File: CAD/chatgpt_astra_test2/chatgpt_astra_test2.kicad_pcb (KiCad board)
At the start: 4 copper layers, 100 x 80 mm, 97 parts, among them J1 18-30 V DC, J2 CURRENT INPUT, J3 CURRENT OUTPUT, J4 USB-C, J5 UART / 3.3 V ONLY, Q1 2N7002, Q2 2N7002, Q3 IRF9540NPBF, Q4 MMBT3906, SW1 RESET, SW2 BOOT, U1 TPS26600PWPR, U10 ADS1115IDGSR, U11 DAC80501ZDGSR, U12 XTR111AIDGQR, U2 LMR36510ADDAR, U3 LT3092EST#PBF, U4 ESP32-S3-WROOM-1-N8, U5 TPS3839G33DBZR, U6 USBLC6-2SC6, U7 LT3092EST#PBF, U8 LM4040AIM3-3.0, U9 TMUX1511PWR

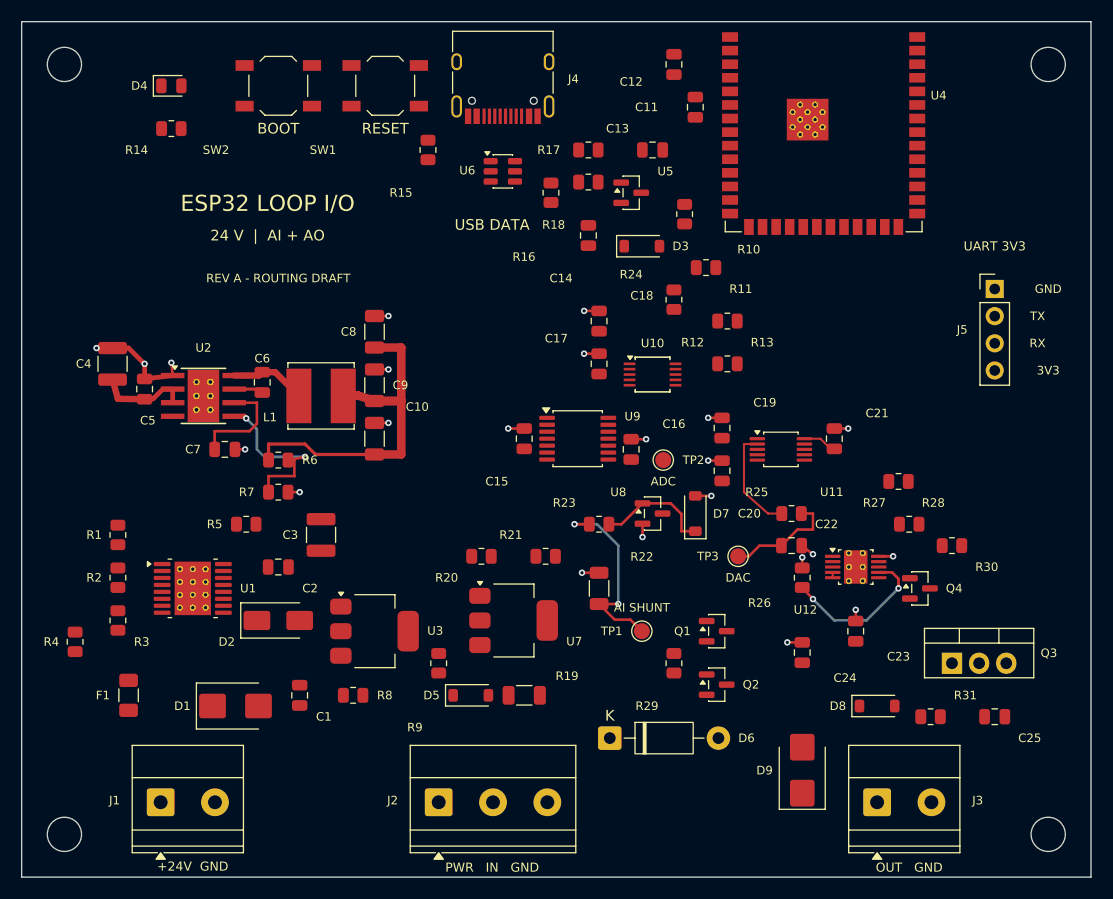
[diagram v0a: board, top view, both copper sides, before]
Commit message: Route remaining board networks with protected analog paths
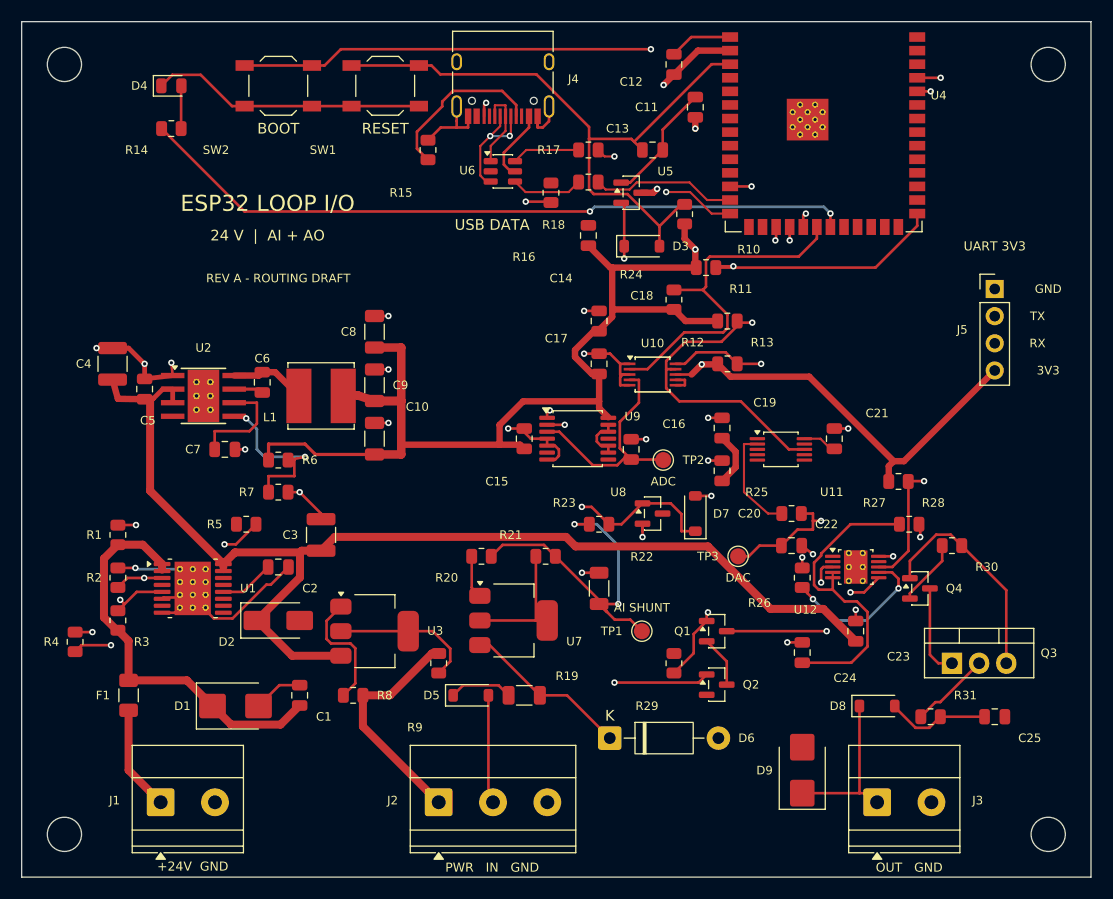
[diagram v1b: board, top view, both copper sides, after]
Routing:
- net V3V3: track 34.8 -> 188.3 mm, vias 0 -> 5
- net V24_PROT: track 8.63 -> 109.1 mm
- net GND: track 37.8 -> 124.8 mm
- net /03 / ESP32 AND USB/BOOT_N: track 0.00 -> 85.4 mm, vias 0 -> 2
- net /03 / ESP32 AND USB/LED_STATUS: track 0.00 -> 67.5 mm, vias 0 -> 2
- net /03 / ESP32 AND USB/ESP_EN: track 0.00 -> 60.9 mm
- net SYS_OK: track 0.00 -> 60.1 mm, vias 0 -> 3
- net /02 / POWER AND SENSOR SUPPLY/EF_RTN: track 0.00 -> 52.5 mm, vias 0 -> 3
- net AO_ENABLE: track 0.00 -> 46.4 mm, vias 0 -> 2
- net I2C_SDA: track 0.00 -> 43.4 mm, vias 0 -> 2
- net AO_FAULT_N: track 0.00 -> 42.4 mm, vias 0 -> 2
- net /02 / POWER AND SENSOR SUPPLY/VIN_FUSED: track 0.00 -> 38.2 mm
- net ADC_RDY: track 0.00 -> 33.1 mm
- net /05 / PRECISION CURRENT OUTPUT/XTR_GATE: track 0.00 -> 29.4 mm, vias 0 -> 1
- net /05 / PRECISION CURRENT OUTPUT/XTR_REG: track 0.50 -> 29.3 mm
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
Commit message: Add D2 ground stitch and document remaining layout work
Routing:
- net GND: track 124.8 -> 125.9 mm, vias 23 -> 24
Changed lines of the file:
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@@
+	)
+	(segment
+		(start 76 106)
+		(end 77.1 106)
+		(width 0.2)
+		(layer "F.Cu")
+		(net 52)
 	)
 	(segment
@@
 		(size 0.6)
 		(drill 0.3)
+		(layers "F.Cu" "B.Cu")
+		(net 52)
+	)
+	(via
+		(at 77.1 106)
+		(size 0.6)
+		(drill 0.3)

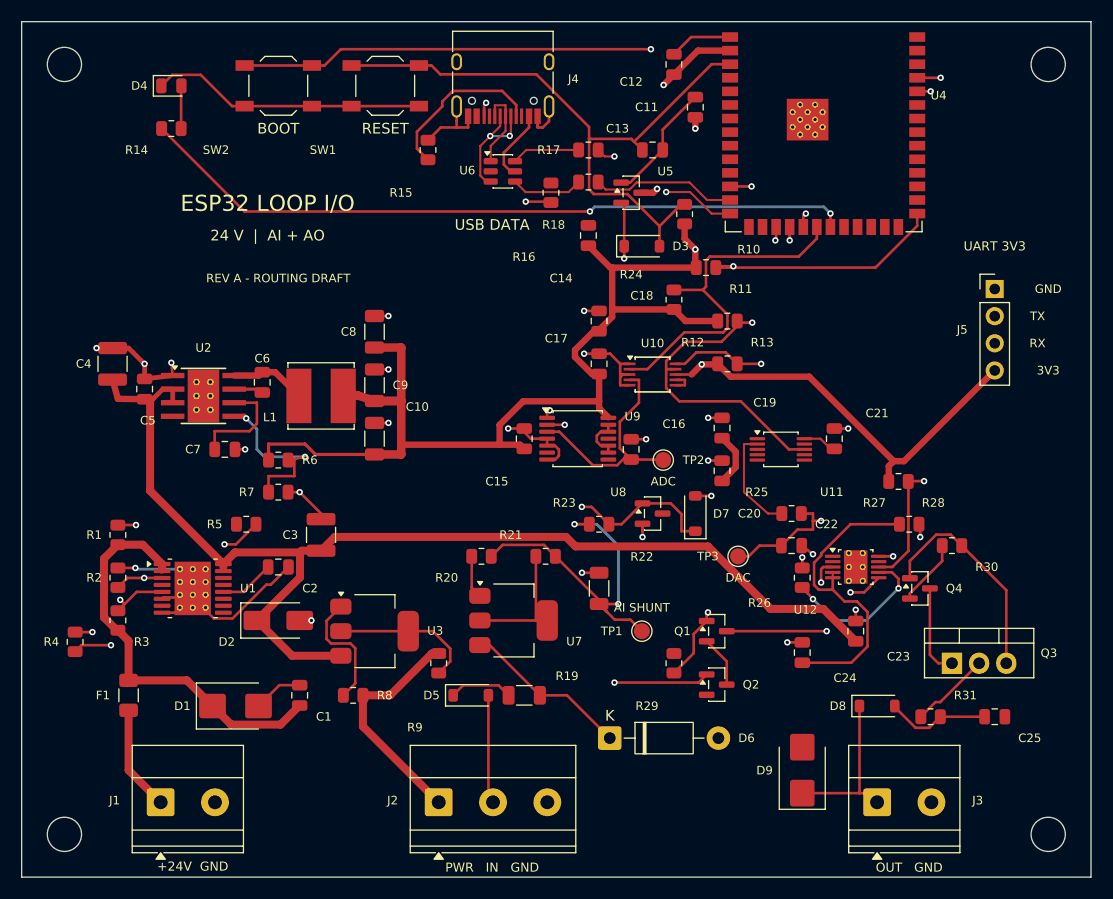
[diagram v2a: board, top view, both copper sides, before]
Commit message: Complete PCB connectivity and resolve local pin escapes
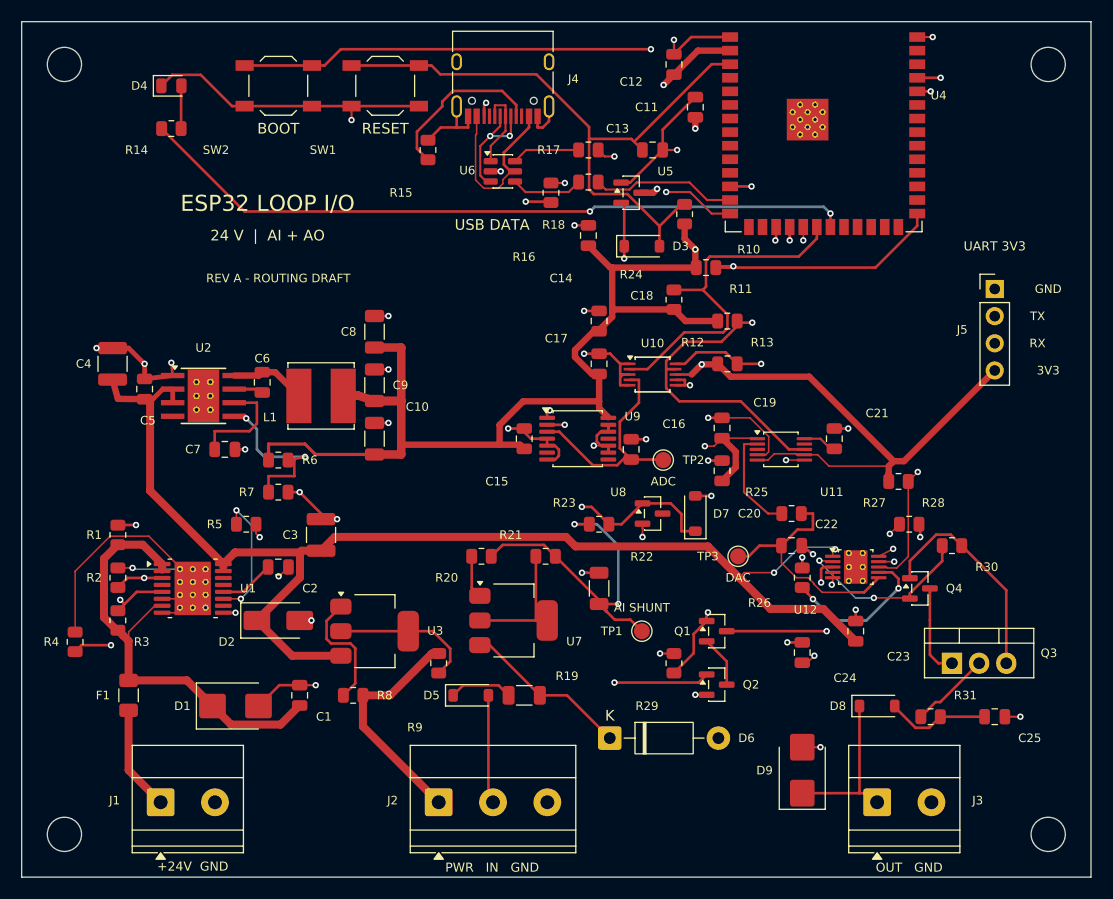
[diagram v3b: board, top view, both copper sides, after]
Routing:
- net GND: track 125.9 -> 155.5 mm, vias 24 -> 40
- net V3V3: track 188.3 -> 215.1 mm, vias 5 -> 6
- net /02 / POWER AND SENSOR SUPPLY/EF_ILIM: track 0.00 -> 12.2 mm, vias 0 -> 2
- net /05 / PRECISION CURRENT OUTPUT/XTR_IS: track 6.20 -> 18.4 mm, vias 0 -> 2
- net I2C_SCL: track 22.3 -> 34.0 mm, vias 2 -> 3
- net V24_PROT: track 109.1 -> 120.1 mm, vias 0 -> 2
- net /03 / ESP32 AND USB/USB_VBUS: track 6.81 -> 17.3 mm
- net /05 / PRECISION CURRENT OUTPUT/XTR_REG: track 29.3 -> 21.3 mm, vias 0 -> 3
- net /02 / POWER AND SENSOR SUPPLY/VIN_FUSED: track 38.2 -> 44.3 mm
- net AO_FAULT_N: track 42.4 -> 38.9 mm
- net /05 / PRECISION CURRENT OUTPUT/XTR_GATE: track 29.4 -> 32.3 mm
- net /05 / PRECISION CURRENT OUTPUT/XTR_OD: track 23.2 -> 24.9 mm, vias 2 -> 3
- net /02 / POWER AND SENSOR SUPPLY/EF_RTN: track 52.5 -> 54.2 mm
- net /05 / PRECISION CURRENT OUTPUT/AO_DRAIN: track 7.52 -> 8.81 mm
- net AO_ENABLE: track 46.4 -> 47.6 mm
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
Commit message: Refine USB pair and add prototype thermal copper and stackup
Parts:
- moved R10 26.0 mm to (137.0, 75.0), turned to 0 degrees
- moved R17 11.7 mm to (112.5, 68.8)
- moved R18 9.53 mm to (112.5, 65.8)
- moved U5 9.00 mm to (107.0, 75.0)
- moved R16 4.50 mm to (99.5, 70.5)
- moved C14 3.49 mm to (103.8, 73.4)
- moved D3 1.28 mm to (109.0, 71.8)
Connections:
- U6 pad 1: /03 / ESP32 AND USB/USB_DP -> /03 / ESP32 AND USB/USB_DM
- U6 pad 3: /03 / ESP32 AND USB/USB_DM -> /03 / ESP32 AND USB/USB_DP
- U6 pad 4: /03 / ESP32 AND USB/USB_DM_ESD -> /03 / ESP32 AND USB/USB_DP_ESD
- U6 pad 6: /03 / ESP32 AND USB/USB_DP_ESD -> /03 / ESP32 AND USB/USB_DM_ESD
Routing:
- net /03 / ESP32 AND USB/ESP_EN: track 60.9 -> 83.8 mm, vias 0 -> 2
- net /03 / ESP32 AND USB/USB_DM_ESD: track 6.75 -> 20.0 mm
- net /03 / ESP32 AND USB/USB_DP_MCU: track 15.1 -> 3.19 mm, vias 2 -> 0
- net /03 / ESP32 AND USB/USB_DP_ESD: track 6.39 -> 17.0 mm
- net /03 / ESP32 AND USB/USB_DM_MCU: track 13.6 -> 3.20 mm
- net /03 / ESP32 AND USB/USB_VBUS: track 17.3 -> 11.9 mm
- net /03 / ESP32 AND USB/USB_DP: track 7.83 -> 12.8 mm, vias 0 -> 3
- net /03 / ESP32 AND USB/USB_CC2: track 14.5 -> 19.3 mm
- net SYS_OK: track 60.6 -> 58.5 mm
- net /03 / ESP32 AND USB/BOOT_N: track 85.4 -> 83.8 mm
- net V3V3: track 215.1 -> 213.8 mm, vias 6 -> 4
- net GND: track 155.5 -> 154.7 mm, vias 40 -> 42
- net /05 / PRECISION CURRENT OUTPUT/XTR_REG: track 21.3 -> 21.9 mm
- net AO_FAULT_N: track 38.9 -> 39.5 mm
- net /03 / ESP32 AND USB/USB_DM: track 11.2 -> 10.7 mm, vias 2 -> 3
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- added copper zone on B.Cu, net /02 / POWER AND SENSOR SUPPLY/EF_RTN
- added copper zone on B.Cu, net /02 / POWER AND SENSOR SUPPLY/SENS_RAW
- added copper zone on F.Cu, net /02 / POWER AND SENSOR SUPPLY/SENS_RAW
- added copper zone on B.Cu, net /04 / PROTECTED CURRENT INPUT/AI_LIMIT_OUT
- added copper zone on F.Cu, net /04 / PROTECTED CURRENT INPUT/AI_LIMIT_OUT
- added copper zone on In2.Cu, net GND
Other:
- board text added: "REV A - PROTOTYPE"
- board text removed: "REV A - ROUTING DRAFT"
